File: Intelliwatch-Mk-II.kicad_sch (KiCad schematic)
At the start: 0 parts

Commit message: WIP op-amp voltage comparator for battery level checking
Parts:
- added C1: 100u, symbol Device:C_Polarized_US
- added C2, C3: 4.7u, symbol Device:C_Polarized_US
- added D1: 1N5817, symbol Device:D_Schottky_Filled
- added DCBatterySupply: Barrel_Jack_MountingPin, Connector_BarrelJack:BarrelJack_Horizontal, symbol Connector:Barrel_Jack_MountingPin
- added J2: USB_C_Receptacle_USB2.0_16P, symbol Connector:USB_C_Receptacle_USB2.0_16P
- added R2: 10k, symbol Device:R_US
- added U1: ESP32-WROOM-32UE, RF_Module:ESP32-WROOM-32UE, symbol RF_Module:ESP32-WROOM-32UE
- added U2: CH340C, Package_SO:SOIC-16_3.9x9.9mm_P1.27mm, symbol Interface_USB:CH340C
- added U3: LM7805, PCM_Package_TO_SOT_THT_AKL:TO-220-3_Vertical, symbol PCM_Voltage_Regulator_AKL:LM7805CT
- added U4: LM1117T-3.3, PCM_Package_TO_SOT_THT_AKL:TO-220-3_Vertical, symbol Regulator_Linear:LM1117T-3.3
- added U5: LM324N, PCM_Package_DIP_AKL:DIP-14_W7.62mm_LongPads, symbol PCM_Amplifier_Operational_AKL:LM324N
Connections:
- new net: D1.2 (A), DCBatterySupply.1
- new net: U1.1 (GND), U1.15 (GND), U1.38 (GND), U1.39 (GND)
- new net: J2.A1 (GND), J2.A12 (GND), J2.B1 (GND), J2.B12 (GND)
- new net: J2.A4 (VBUS), J2.A9 (VBUS), J2.B4 (VBUS), J2.B9 (VBUS)
- new net +3V3: C3.1, U4.2 (VO)
- new net +5V: C2.1, U3.3 (OUT), U4.3 (VI), U5.2 (-)
- new net +BATT: C1.1, D1.1 (K), R2.1, U3.1 (IN), U5.3 (+), U5.4 (V+)
- new net BatteryLevel: R2.2, U5.1
- new net GNDREF: C1.2, C2.2, C3.2, DCBatterySupply.2, DCBatterySupply.MP (MountPin), U3.2, U4.1 (GND), U5.11 (V-)
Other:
- note added: "Batt: 2x 3.7V MAX: 8.4 V AVG: 7.4 V MIN: 5.6 V"
- note added: "TODO: figure out how to shift BATT and 5V onto ground reference"

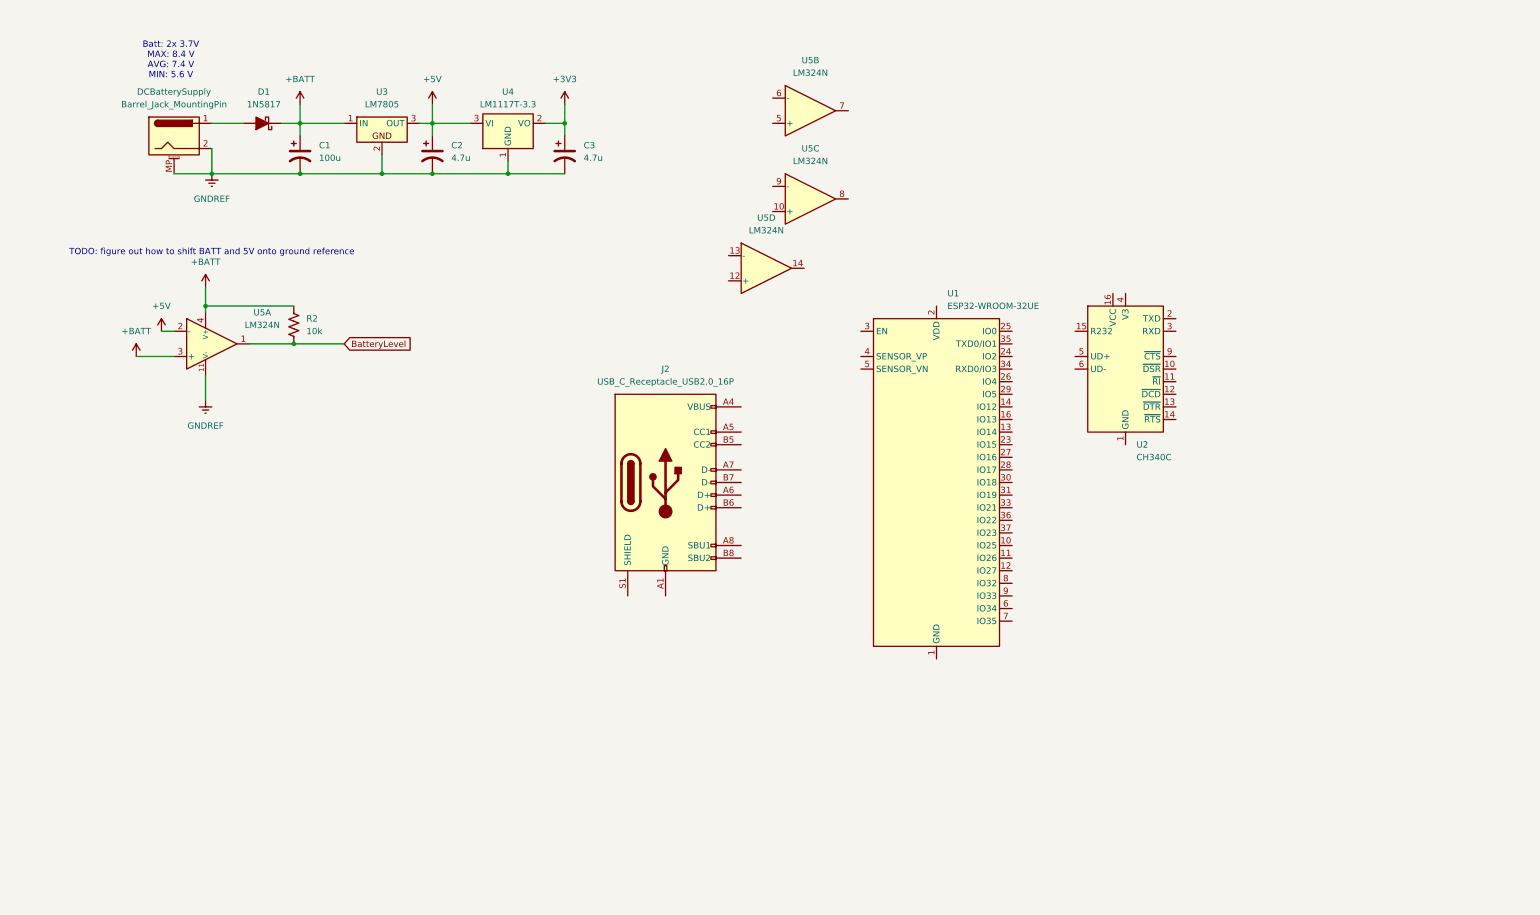
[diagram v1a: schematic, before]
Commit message: connected USB-C to SERIAL-UART adapter.
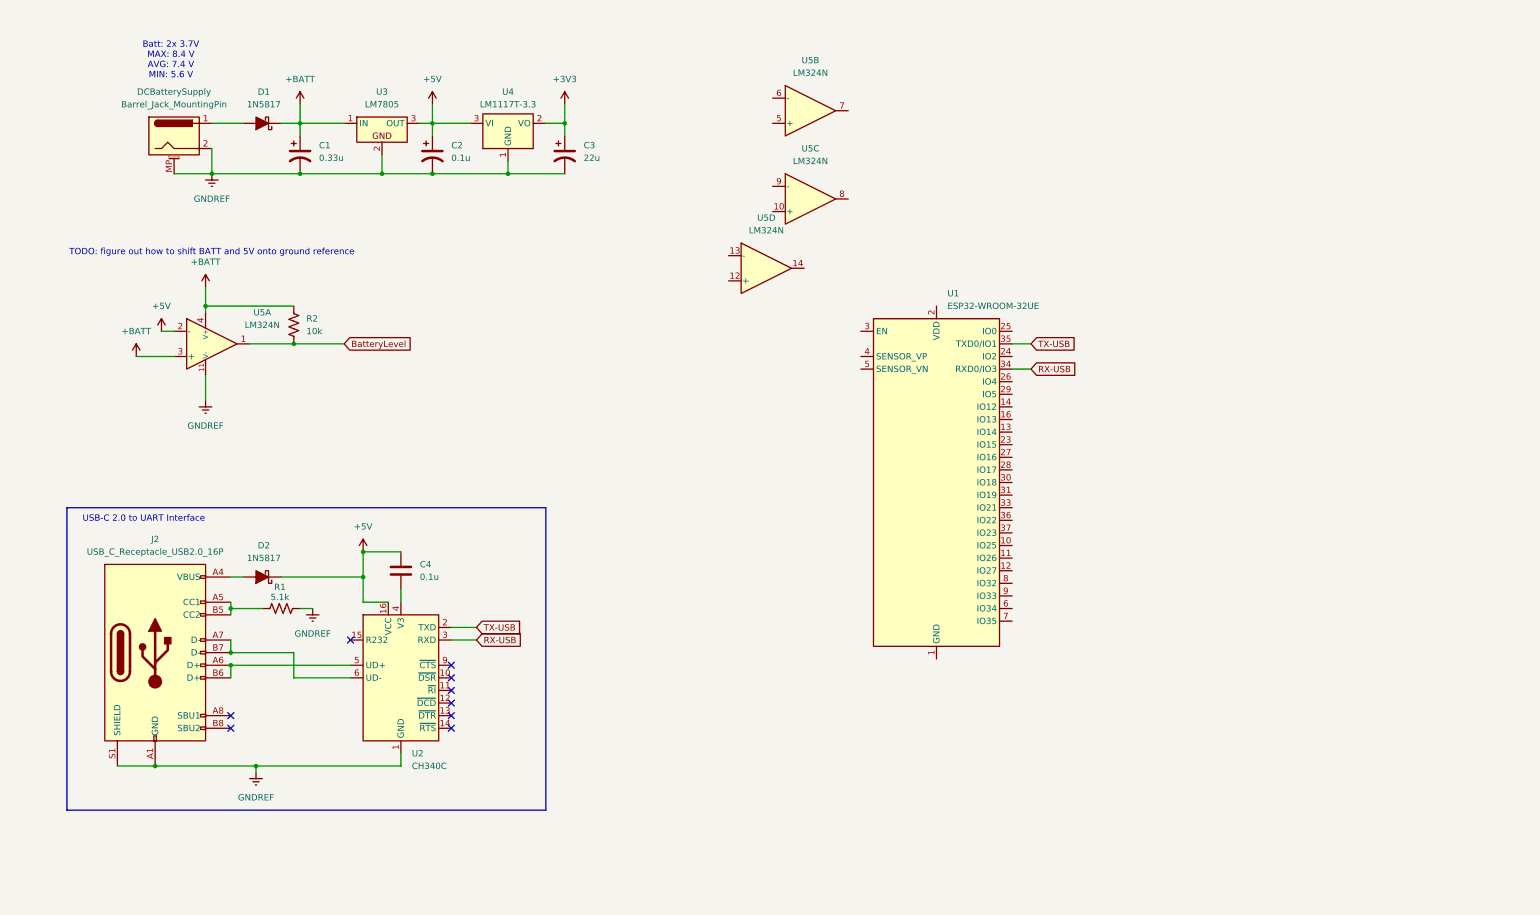
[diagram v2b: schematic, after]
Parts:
- added C4: 0.1u, symbol Device:C
- added D2: 1N5817, symbol Device:D_Schottky_Filled
- added R1: 5.1k, symbol Device:R_US
- C1: value 100u -> 0.33u
- C2: value 4.7u -> 0.1u
- C3: value 4.7u -> 22u
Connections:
- net +5V: now also U2.16 (VCC), C4.1, D2.1 (K)
- net GNDREF: now also J2.A1 (GND), J2.A12 (GND), J2.B1 (GND), J2.B12 (GND), J2.S1 (SHIELD), U2.1 (GND), R1.2
- net RX-USB: now reaches U1.34 (RXD0/IO3)
- net RX-USB: now also U2.3 (RXD)
- net TX-USB: now reaches U1.35 (TXD0/IO1)
- net TX-USB: now also U2.2 (TXD)
- net at U2.4 (V3): now also C4.2
- net at U2.5 (UD+): now also J2.A6 (D+), J2.B6 (D+)
- net at U2.6 (UD-): now also J2.A7 (D-), J2.B7 (D-)
- net at J2.A4 (VBUS), J2.A9 (VBUS), J2.B4 (VBUS)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: now also D2.2 (A)
- net at J2.A5 (CC1): now also J2.B5 (CC2), R1.1
- no-connect marks 0 -> 9
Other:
- note added: "USB-C 2.0 to UART Interface"
- moved on the sheet: J2, U2

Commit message: ADDED QMC5883L IC, imported, then assigned some footprints
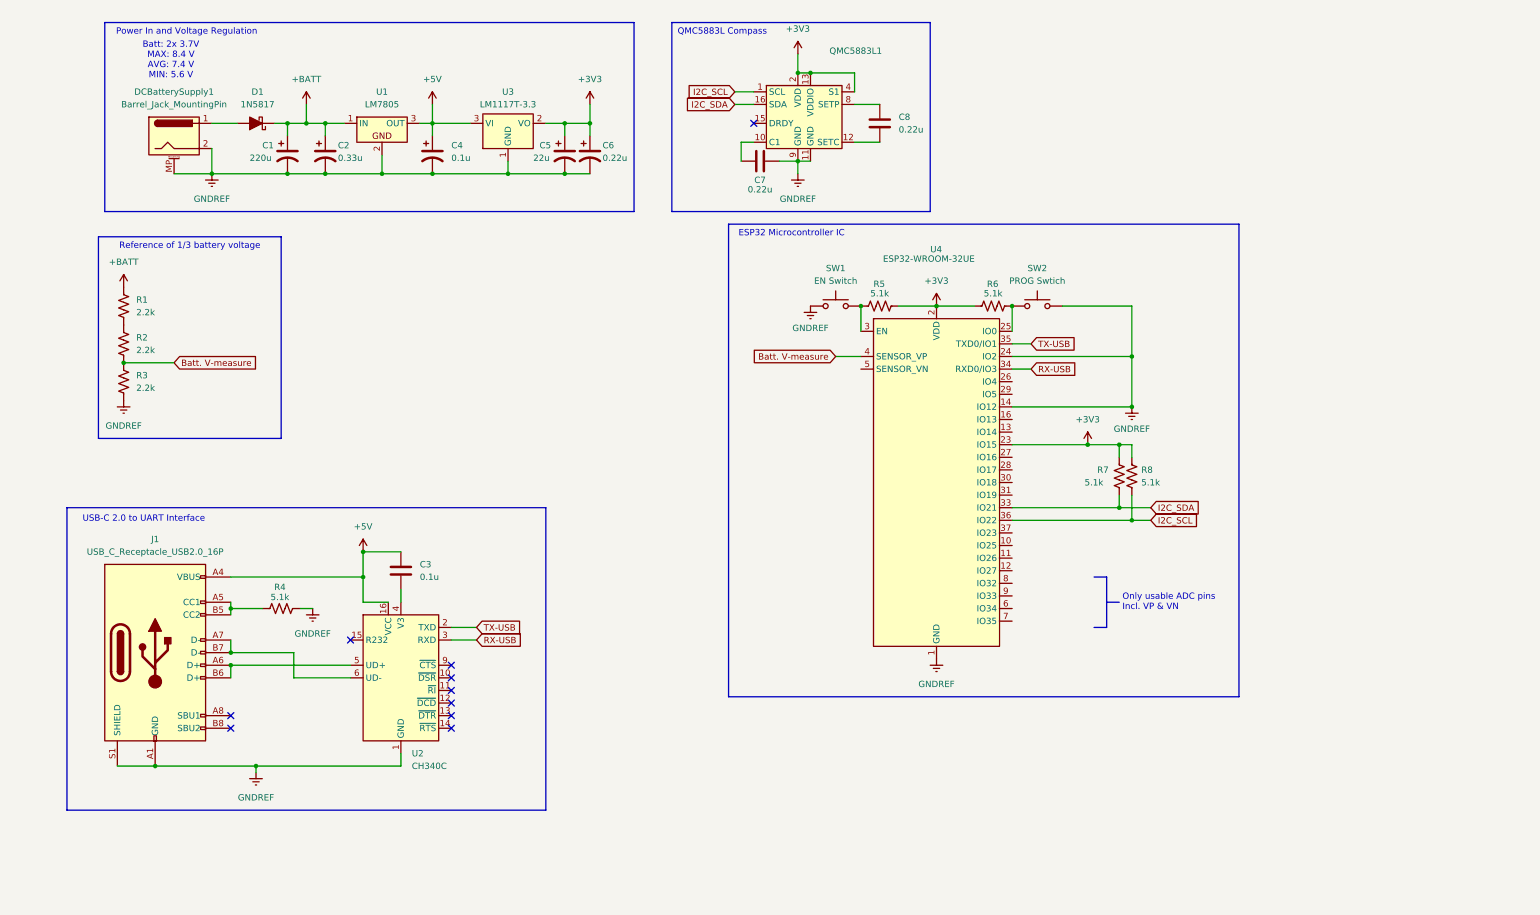
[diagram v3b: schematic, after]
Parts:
- removed D2: 1N5817, symbol Device:D_Schottky_Filled
- removed U5: LM324N, PCM_Package_DIP_AKL:DIP-14_W7.62mm_LongPads, symbol PCM_Amplifier_Operational_AKL:LM324N
- added C1: 220u, symbol Device:C_Polarized_US
- added C6: 0.22u, symbol Device:C_Polarized_US
- added C7, C8: 0.22u, symbol Device:C
- added QMC5883L1: ~, Package_LGA:LGA-16_3x3mm_P0.5mm, symbol ZCustomSymbols:QMC5883L Compass IC
- added R1, R3: 2.2k, symbol Device:R_US
- added R5, R6, R7, R8: 5.1k, symbol Device:R_US
- added SW1: EN Switch, TS-1101-C-W Switch:SW_101-C-W_XKB, symbol Switch:SW_Push
- added SW2: PROG Swtich, TS-1101-C-W Switch:SW_101-C-W_XKB, symbol Switch:SW_Push
- J1: renamed from J2; footprint (none) -> Connector_USB:USB_C_Receptacle_G-Switch_GT-USB-7010ASV
- R2: value 10k -> 2.2k
- renumbered C1 to C2, C4 to C3, C2 to C4, C3 to C5, DCBatterySupply to DCBatterySupply1, R1 to R4, U3 to U1, U4 to U3, U1 to U4
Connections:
- net BatteryLevel is gone; now on net Batt. V-measure: R2.2
- net +3V3: now also U4.2 (VDD), U4.23 (IO15), C6.1, QMC5883L1.13 (VDDIO), QMC5883L1.2 (VDD), QMC5883L1.4 (S1), R5.1, R6.2, R7.1, R8.1
- net +5V: now also J1.A4 (VBUS), J1.A9 (VBUS), J1.B4 (VBUS), J1.B9 (VBUS)
- net +BATT: now also C1.1, R1.1; no longer R2.1
- net GNDREF: now also U4.1 (GND), U4.14 (IO12), U4.15 (GND), U4.24 (IO2), U4.38 (GND), U4.39 (GND), C1.2, C6.2, C7.2, QMC5883L1.11 (GND), QMC5883L1.9 (GND), R3.2, SW1.1, SW2.2
- net at U4.25 (IO0): now also R6.1, SW2.1
- net at U4.3 (EN): now also R5.2, SW1.2
- net I2C_SDA: now reaches U4.33 (IO21)
- net I2C_SDA: now also QMC5883L1.16 (SDA), R7.2
- net I2C_SCL: now reaches U4.36 (IO22)
- net I2C_SCL: now also QMC5883L1.1 (SCL), R8.2
- net Batt. V-measure: now reaches U4.4 (SENSOR_VP)
- net Batt. V-measure: now also R3.1
- new net: C7.1, QMC5883L1.10 (C1)
- new net: C8.2, QMC5883L1.12 (SETC)
- new net: C8.1, QMC5883L1.8 (SETP)
- new net: R1.2, R2.1
- no-connect marks 9 -> 10
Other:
- note added: "ESP32 Microcontroller IC"
- note added: "Only usable ADC pins Incl. VP & VN"
- note added: "Power In and Voltage Regulation"
- note added: "QMC5883L Compass"
- note added: "Reference of 1/3 battery voltage"
- note removed: "TODO: figure out how to shift BATT and 5V onto ground reference"
- moved on the sheet: C2, D1

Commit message: Made capacitor values more uniform. TODO is add auto-flash support from DTR and RTS pins on SERIAL-UART converter IC.
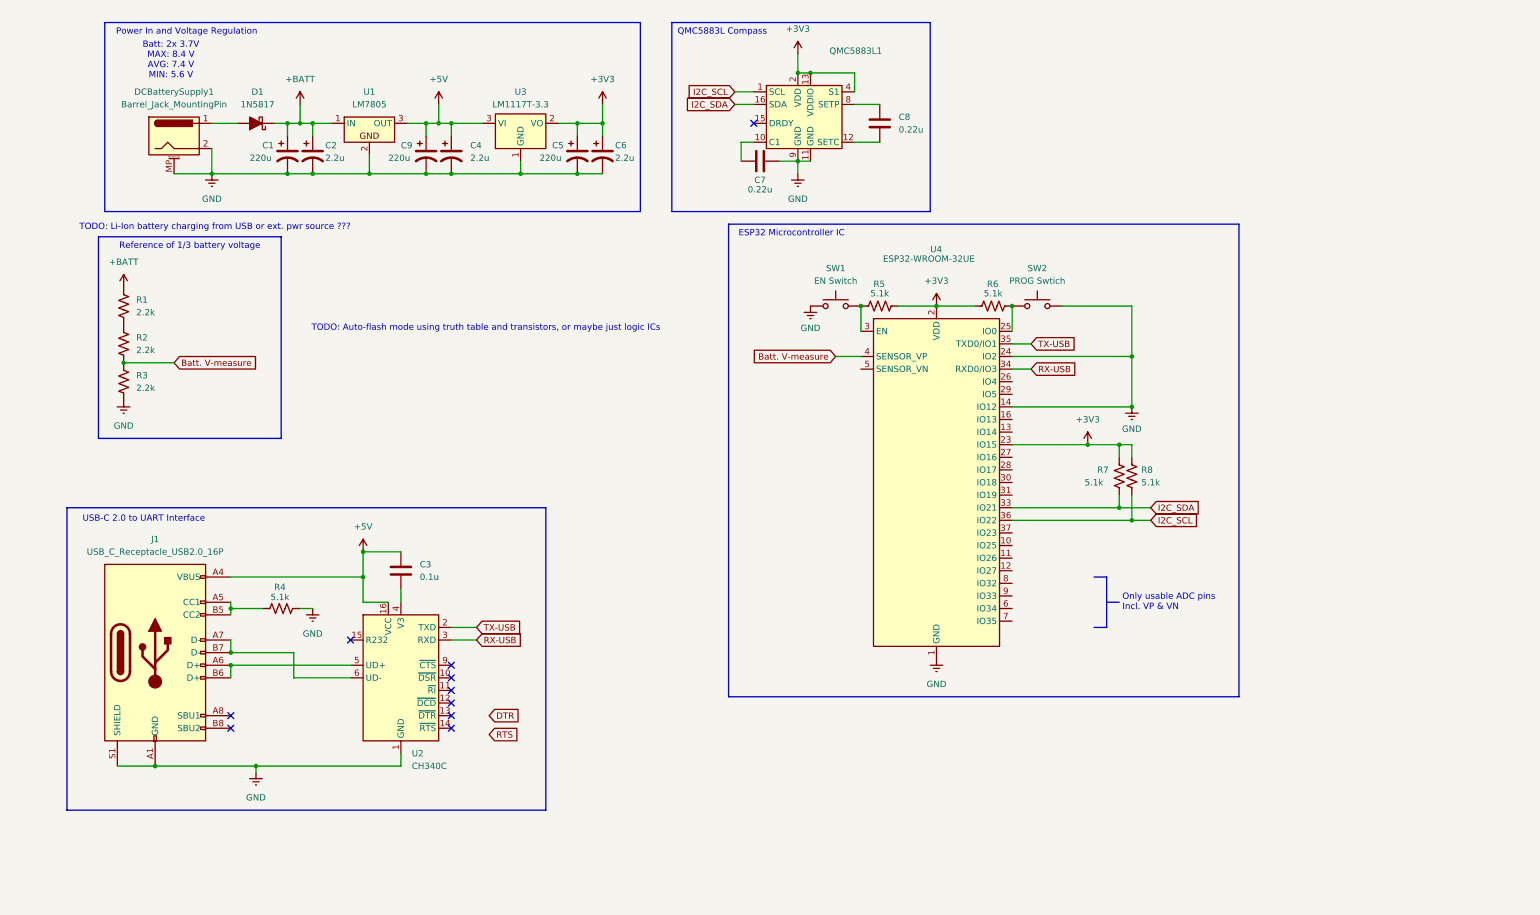
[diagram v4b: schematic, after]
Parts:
- added C9: 220u, symbol Device:C_Polarized_US
- C2: value 0.33u -> 2.2u
- C4: value 0.1u -> 2.2u
- C5: value 22u -> 220u
- C6: value 0.22u -> 2.2u
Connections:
- net +5V: now also C9.1
- net GNDREF renamed GND
- net GND: now also C9.2
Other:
- note added: "TODO: Auto-flash mode using truth table and transistors, or maybe just logic ICs"
- note added: "TODO: Li-Ion battery charging from USB or ext. pwr source ???"
- moved on the sheet: C2, C4, C6, U1, U3

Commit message: ADDED all the damn logic for automatically pulling the EN and IO0 pins into flash-mode on the ESP32 depending on RTS and DTR serial signals.
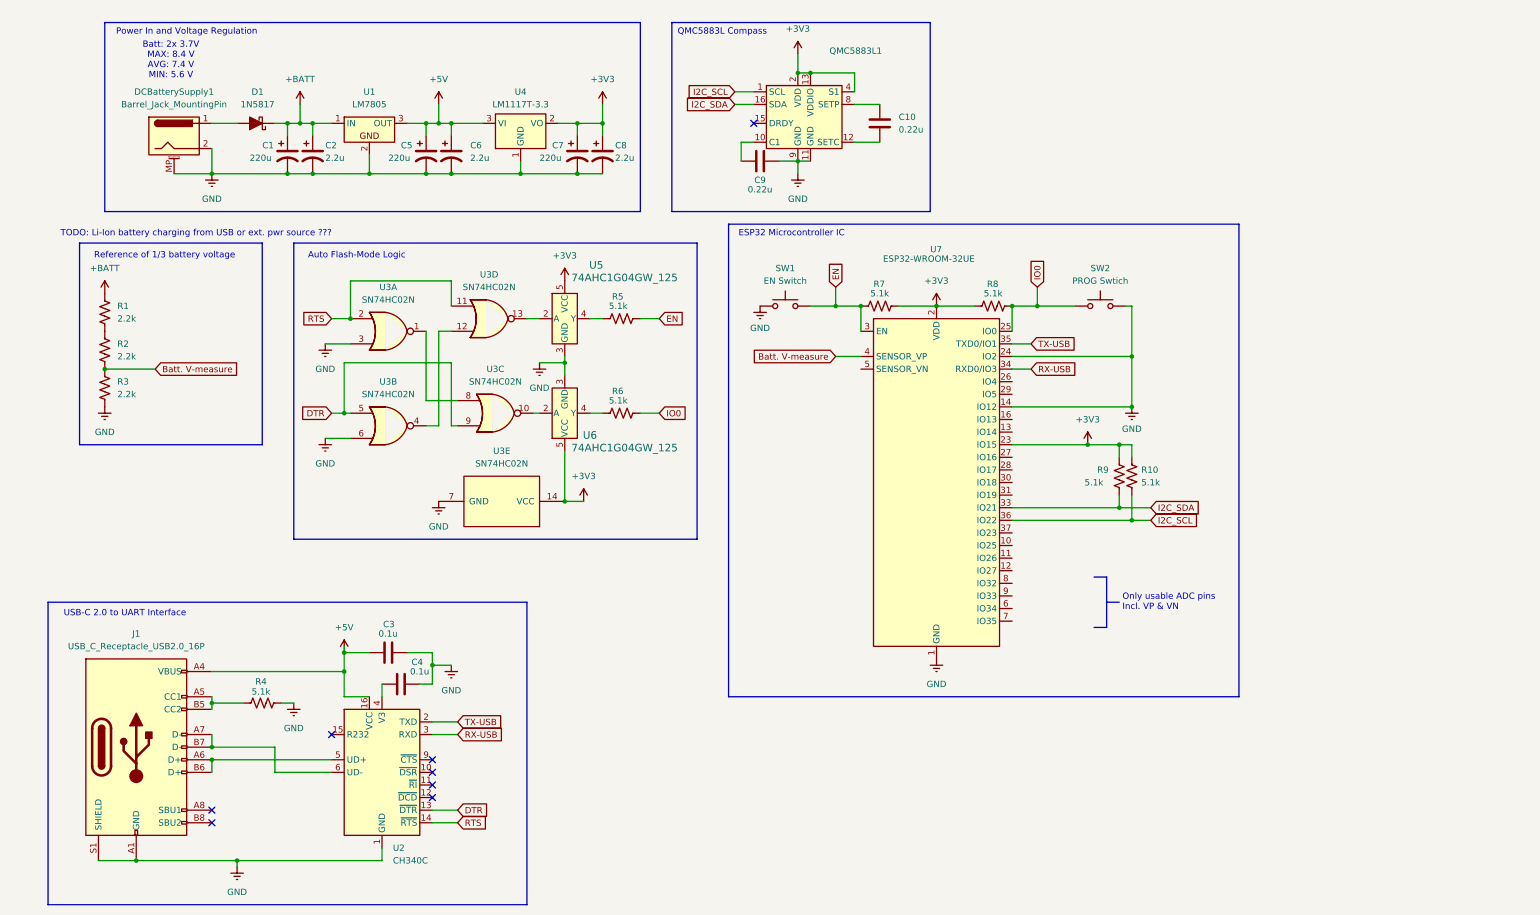
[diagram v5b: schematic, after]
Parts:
- added C3: 0.1u, symbol Device:C
- added R5, R6: 5.1k, symbol Device:R_US
- added U3: SN74HC02N, Package_DIP:DIP-14_W7.62mm, symbol 74xx:74HC02
- added U5, U6: 74AHC1G04GW_125, Package_TO_SOT_SMD:SOT-353_SC-70-5, symbol 74AHC1G04GV,125:74AHC1G04GW_125
- renumbered C8 to C10, C3 to C4, C9 to C5, C4 to C6, C5 to C7, C6 to C8, C7 to C9, R8 to R10, R5 to R7, R6 to R8, R7 to R9, U3 to U4, U4 to U7
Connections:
- net +3V3: now also U3.14 (VCC), U5.5 (VCC), U6.5 (VCC)
- net +5V: now also C3.1; no longer C4.1
- net DTR: now also U2.13 (~{DTR}), U3.5, U3.9
- net GND: now also C4.2, C3.2, U3.3, U3.6, U3.7 (GND), U5.3 (GND), U6.3 (GND)
- net RTS: now also U2.14 (~{RTS}), U3.11, U3.2
- net IO0: now reaches R8.1, SW2.1, U7.25 (IO0)
- net IO0: now also R6.1
- net EN: now reaches R7.2, SW1.2, U7.3 (EN)
- net EN: now also R5.1
- net at U2.4 (V3): now also C4.1; no longer C4.2
- new net: U3.1, U3.8
- new net: U3.10, U6.2 (A)
- new net: R6.2, U6.4 (Y)
- new net: U3.12, U3.4
- new net: U3.13, U5.2 (A)
- new net: R5.2, U5.4 (Y)
- no-connect marks 10 -> 8
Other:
- note added: "Auto Flash-Mode Logic"
- note removed: "TODO: Auto-flash mode using truth table and transistors, or maybe just logic ICs"
- moved on the sheet: C4, J1, R1, R2, R3, R4, SW1, SW2, U2
